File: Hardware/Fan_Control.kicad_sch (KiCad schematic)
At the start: 20 parts, among them Q1 PSMN8R5-40MSDX, Q3 PSMN8R5-40MSDX, U3 EMC2305-1-AP-TR

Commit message: BPS-Leader Schematic completed (mostly)
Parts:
- removed R14: 5k, symbol Device:R_US
- removed R15: 10k, symbol Device:R_US
- added R31, R35: 10k, Resistor_SMD:R_0603_1608Metric, symbol Device:R_US
- D4, D7: footprint UTSVT_Passive:MMDL101T1G -> UTSVT_Passives:MMDL101T1G
- R1, R13, R16, R17, R5: footprint (none) -> Resistor_SMD:R_0603_1608Metric
- R12: value 5k -> 10k; footprint (none) -> Resistor_SMD:R_0603_1608Metric
- R2: value 33k -> 10k; footprint (none) -> Resistor_SMD:R_0603_1608Metric
- R3, R4: value 10k -> 5k; footprint (none) -> Resistor_SMD:R_0603_1608Metric
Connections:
- net +3.3V: now also R1.2, R12.2, R31.1, R35.1; no longer R1.1, R12.1
- net CLK_PULLUP: now also R13.2; no longer R1.2
- net FAN_1_PWM: now also R12.1; no longer R5.2
- net FAN_1_TACH: now also R3.2; no longer R12.2, U3.6 (TACH1)
- net FAN_2_PWM: now also R1.1; no longer R13.2
- net FAN_2_TACH: now also R4.2; no longer U3.8 (TACH2)
- net FAN_ALERT: now also R5.2
- net FAN_SCL: now also R35.2; no longer R4.2
- net FAN_SDA: now also R31.2; no longer R3.2
- no-connect marks 6 -> 8
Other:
- note added: "Test to see if 100k pulldowns nessasaey"
- note removed: "Allows CLK pin to control fan default; See fig 1-2 for details"
- note removed: "Pull-Up Resistors"
- note removed: "Sets fan default to 50% see fig 1-1 for details"
- moved on the sheet: C1, C2, D4, D7, Fan1, Fan2, Q1, Q3, R16, R17, U3

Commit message: Small tweaks
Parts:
- R16, R17: now not fitted
- U3: footprint FanControl:QFN16_4x4MC_MCH -> (none)
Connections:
- net FAN_1_TACH: now also U3.6 (TACH1)
- net FAN_2_TACH: now also U3.8 (TACH2)
- no-connect marks 8 -> 6
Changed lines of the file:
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@@
 	)
 	(no_connect
-		(at 100.33 49.53)
-	)
-	(no_connect
 		(at 151.13 57.15)
 	)
@@
 		(at 151.13 44.45)
 	)
-	(no_connect
-		(at 100.33 54.61)
-	)
 	(wire
 		(pts
@@
 	(wire
 		(pts
+			(xy 87.63 49.53) (xy 100.33 49.53)
+		)
+		(stroke
+			(width 0)
+			(type default)
+		)
+	)
+	(wire
+		(pts
 			(xy 46.99 135.89) (xy 46.99 138.43)
 		)
@@
 	(wire
 		(pts
+			(xy 87.63 54.61) (xy 100.33 54.61)
+		)
+		(stroke
+			(width 0)
+			(type default)
+		)
+	)
+	(wire
+		(pts
 			(xy 151.13 49.53) (xy 154.94 49.53)
 		)
@@
 		)
 	)
+	(label "FAN_1_TACH"
+		(at 87.63 49.53 0)
+		(effects
+			(font
+				(size 1.27 1.27)
+			)
+			(justify left bottom)
+		)
+	)
 	(label "CLK_PULLUP"
 		(at 182.88 52.07 180)
@@
 		)
 	)
+	(label "FAN_2_TACH"
+		(at 87.63 54.61 0)
+		(effects
+			(font
+				(size 1.27 1.27)
+			)
+			(justify left bottom)
+		)
+	)
 	(label "FAN_1_FLYBACK"
 		(at 31.75 172.72 0)
@@
 			)
 		)
-		(property "Footprint" "FanControl:QFN16_4x4MC_MCH"
+		(property "Footprint" ""
 			(at 100.33 36.83 0)
 			(effects
@@
 		(in_bom yes)
 		(on_board yes)
-		(dnp no)
+		(dnp yes)
 		(fields_autoplaced yes)
 		(property "Reference" "R16"
@@
 		(in_bom yes)
 		(on_board yes)
-		(dnp no)
+		(dnp yes)
 		(fields_autoplaced yes)
 		(property "Reference" "R17"

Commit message: Very, very intial layout designed. Many issues. Too bad!
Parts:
- Fan1, Fan2: footprint (none) -> Connector_Molex:Molex_Nano-Fit_105309-xx03_1x03_P2.50mm_Vertical
- U3: footprint (none) -> SN74HC594DWG4:QFN16_4x4MC_MCH
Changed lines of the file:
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@@
 			)
 		)
-		(property "Footprint" ""
+		(property "Footprint" "Connector_Molex:Molex_Nano-Fit_105309-xx03_1x03_P2.50mm_Vertical"
 			(at 186.69 128.27 0)
 			(effects
@@
 			)
 		)
-		(property "Footprint" ""
+		(property "Footprint" "Connector_Molex:Molex_Nano-Fit_105309-xx03_1x03_P2.50mm_Vertical"
 			(at 250.19 128.27 0)
 			(effects
@@
 			)
 		)
-		(property "Footprint" ""
+		(property "Footprint" "SN74HC594DWG4:QFN16_4x4MC_MCH"
 			(at 100.33 36.83 0)
 			(effects

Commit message: Backup
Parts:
- U3: footprint SN74HC594DWG4:QFN16_4x4MC_MCH -> EMC2305-1-AP-TR:QFN65P400X400X90-17N-D
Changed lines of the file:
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@@
 			)
 		)
-		(property "Footprint" "SN74HC594DWG4:QFN16_4x4MC_MCH"
+		(property "Footprint" "EMC2305-1-AP-TR:QFN65P400X400X90-17N-D"
 			(at 100.33 36.83 0)
 			(effects

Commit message: small fixes
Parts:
- C1, C2: footprint Capacitor_SMD:C_0805_2012Metric -> Capacitor_SMD:C_0603_1608Metric; Manufactuerer (none) -> KEMET
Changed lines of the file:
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@@
 			)
 		)
-		(property "Footprint" "Capacitor_SMD:C_0805_2012Metric"
-			(at 44.45 45.72 0)
-			(effects
-				(font
-					(size 1.27 1.27)
-				)
-				(hide yes)
-			)
-		)
-		(property "Datasheet" "https://www.mouser.com/datasheet/2/447/KEM_C1006_X5R_SMD-3316465.pdf"
+		(property "Footprint" "Capacitor_SMD:C_0603_1608Metric"
+			(at 44.45 45.72 0)
+			(effects
+				(font
+					(size 1.27 1.27)
+				)
+				(hide yes)
+			)
+		)
+		(property "Datasheet" "https://www.mouser.com/datasheet/3/72/1/KEM_C1006_X5R_SMD.pdf"
 			(at 44.45 45.72 0)
 			(effects
@@
 			)
 		)
-		(property "Manufactuerer" ""
+		(property "Manufactuerer" "KEMET "
 			(at 44.45 45.72 0)
 			(effects
@@
 			)
 		)
-		(property "Footprint" "Capacitor_SMD:C_0805_2012Metric"
-			(at 49.53 45.72 0)
-			(effects
-				(font
-					(size 1.27 1.27)
-				)
-				(hide yes)
-			)
-		)
-		(property "Datasheet" "https://www.mouser.com/datasheet/2/447/KEM_C1006_X5R_SMD-3316465.pdf"
+		(property "Footprint" "Capacitor_SMD:C_0603_1608Metric"
+			(at 49.53 45.72 0)
+			(effects
+				(font
+					(size 1.27 1.27)
+				)
+				(hide yes)
+			)
+		)
+		(property "Datasheet" "https://www.mouser.com/datasheet/3/72/1/KEM_C1006_X5R_SMD.pdf"
 			(at 49.53 45.72 0)
 			(effects
@@
 			)
 		)
-		(property "Manufactuerer" ""
-			(at 49.53 45.72 0)
-			(effects
+		(property "Manufactuerer" "KEMET "
+			(at 49.53 45.72 0)
+			(effects

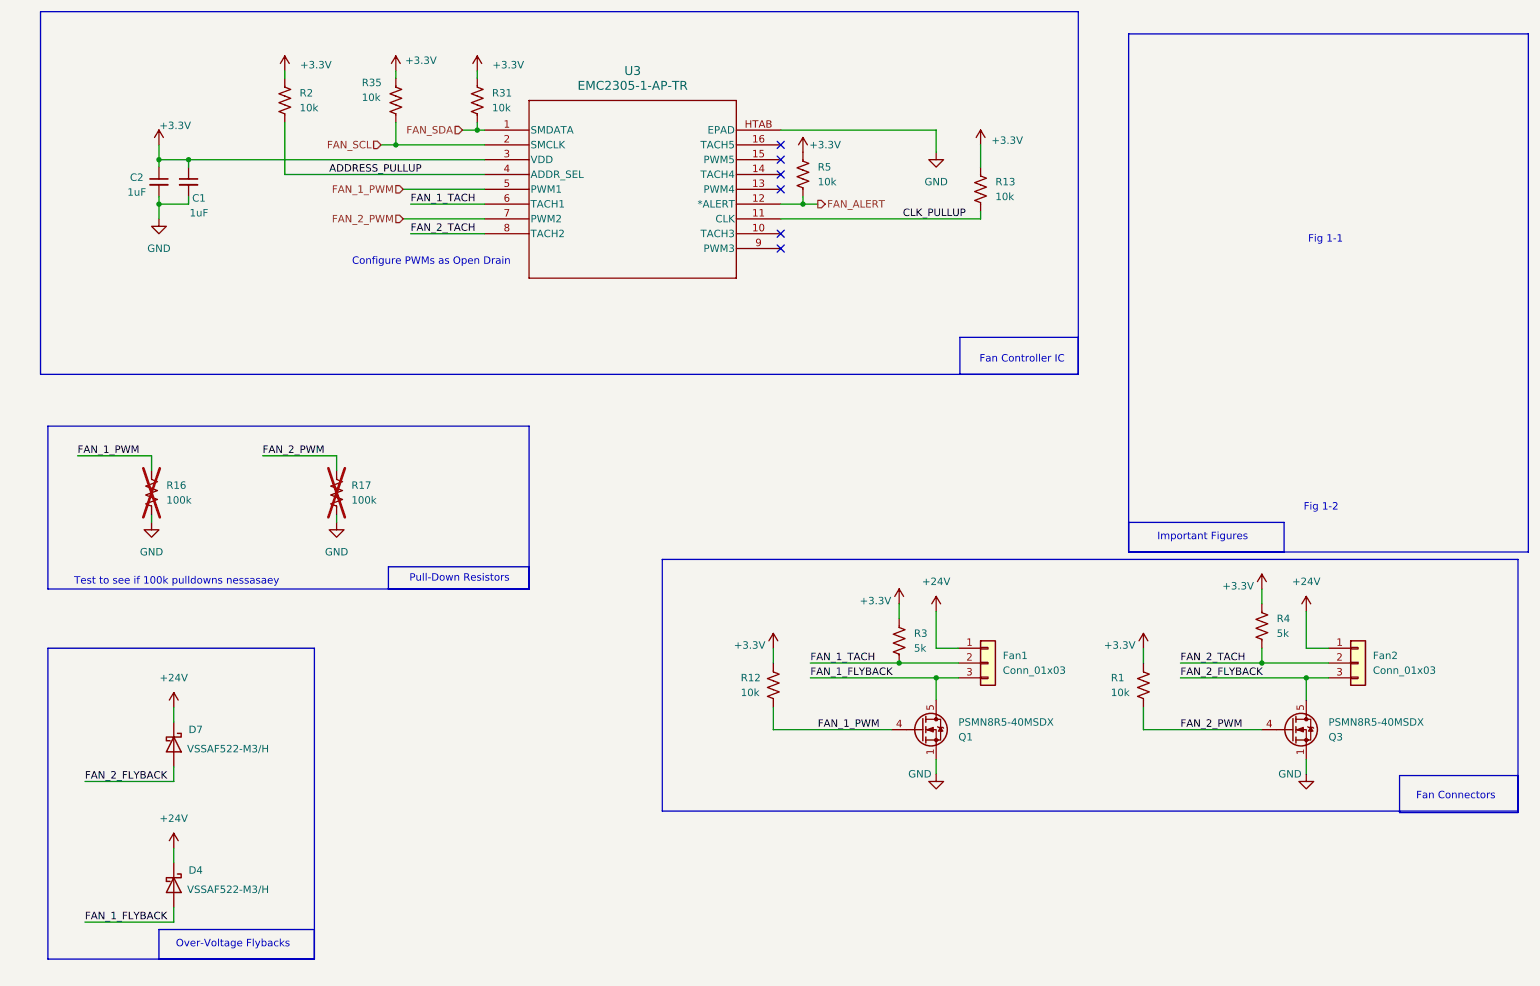
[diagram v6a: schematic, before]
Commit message: added BOM
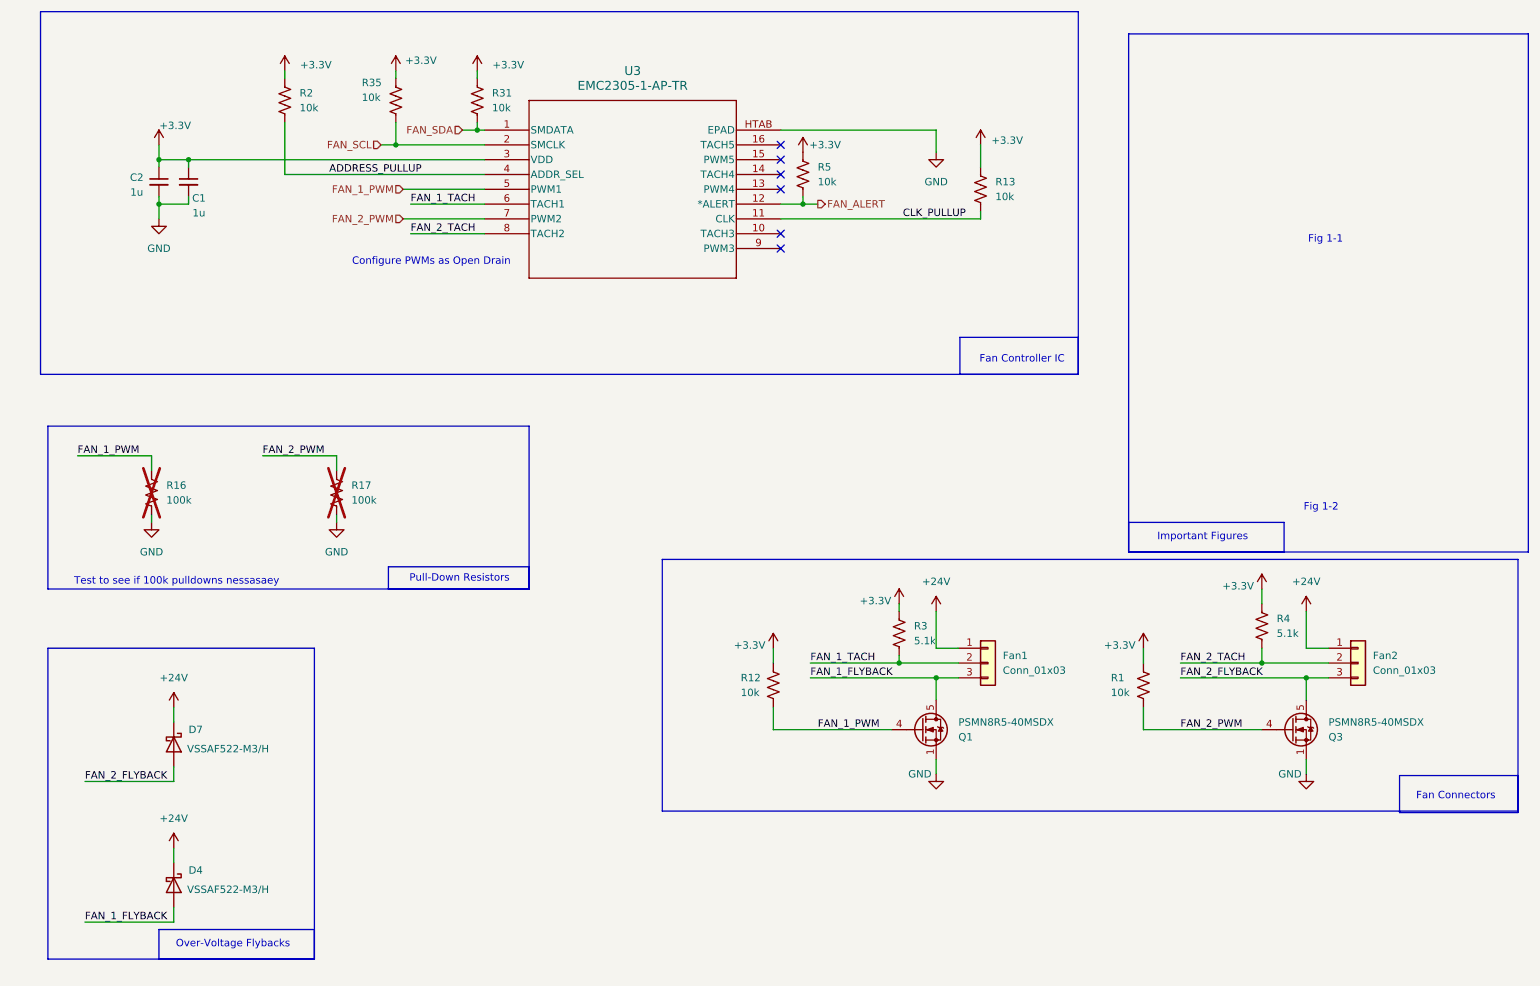
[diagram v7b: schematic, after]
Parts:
- C1, C2: value 1uF -> 1u; Manufactuerer KEMET -> TAIYO YUDEN; P/N C0805C105K5PACTU -> MLASU168SB5105KTNA01
- D4, D7: Manufactuerer (none) -> Vishay General Semiconductor; P/N (none) -> VSSAF522-M3/H
- Fan1, Fan2: Manufactuerer (none) -> Molex; P/N (none) -> 105309-1303
- Q1, Q3: Manufactuerer (none) -> Nexperia; P/N (none) -> PSMN8R5-40MSDX
- R1, R12, R13, R2, R31, R35, R5: Manufactuerer (none) -> Vishay; P/N (none) -> CRCW060310K0FKEI
- R16, R17: Manufactuerer (none) -> Vishay; P/N (none) -> CRCW0603100KFKEE
- R3, R4: value 5k -> 5.1k; Manufactuerer (none) -> Vishay; P/N (none) -> CRCW06035K10FKEC
- U3: Manufactuerer (none) -> Microchip Technology
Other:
- moved on the sheet: R3

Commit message: RevB PR (#14)
* RevB Schematic Update

* RevB Schematic revisions

* revB updates

* Schematic polishes, layout WIP

* circuit blocks designed, schematic updated

* unblocked SD card holder

* halfway laid-out

* unblocked SD card again

* small schematic changes

* intial layout design

* Updated LSOM footprint

* filled in copper holes. Name/REV/Date added

* RevB layout completed

* JLC Production Files

* added resistors

* replace silkscreen

* condensed custom lirbraries

* removed all unnessasary files and some nessasary ones
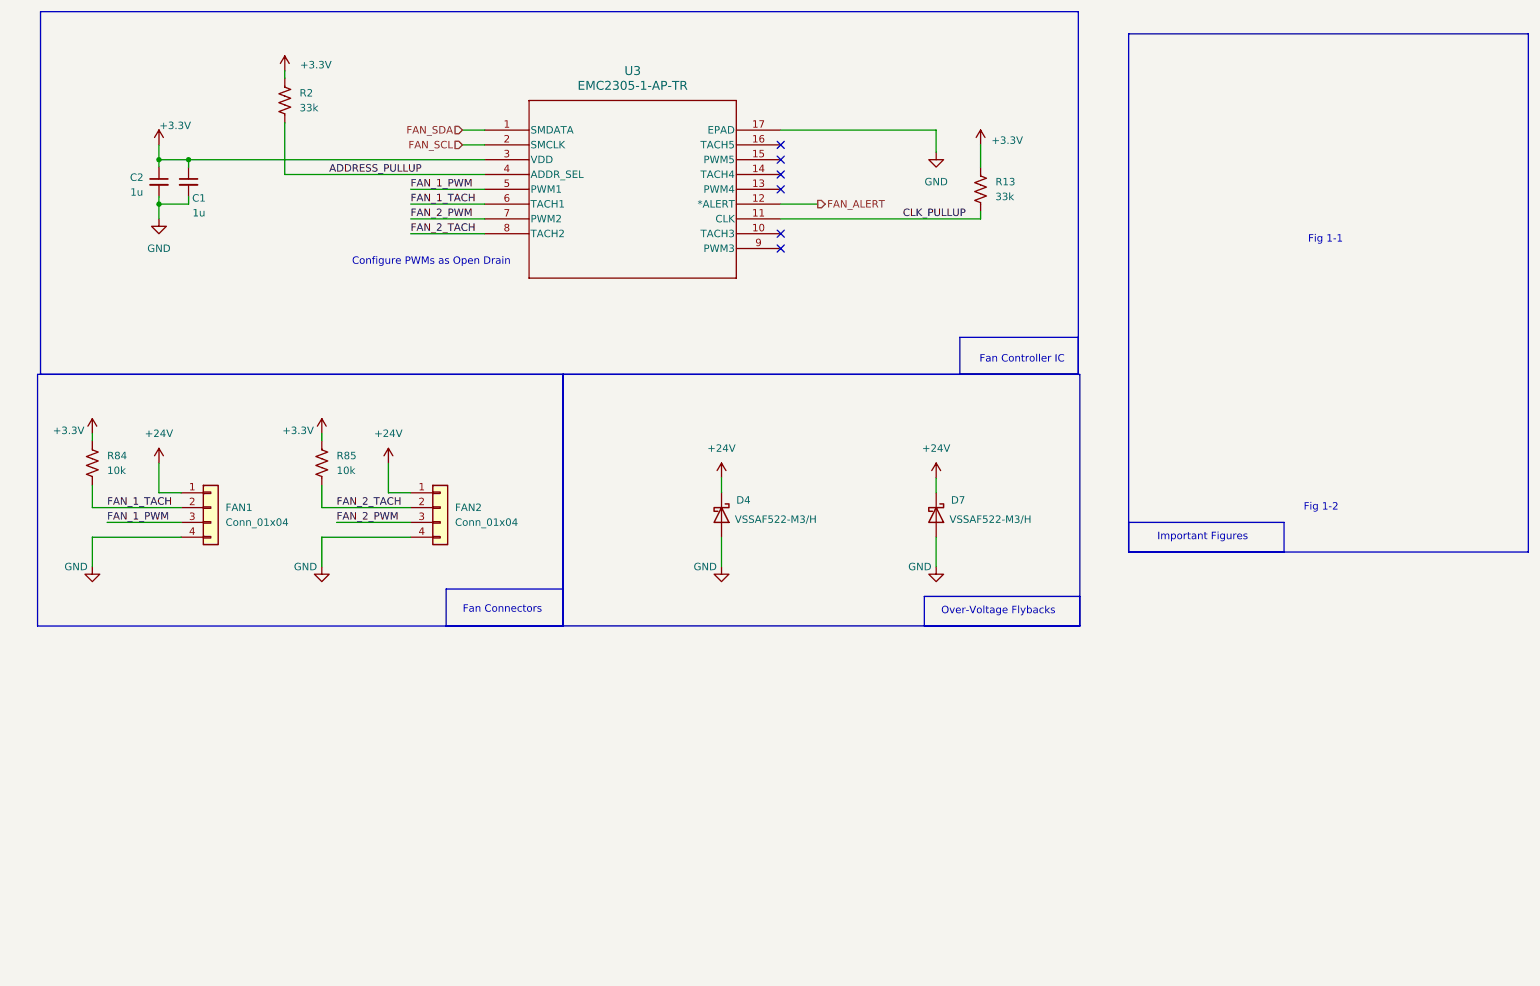
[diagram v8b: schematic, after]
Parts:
- removed Fan1, Fan2: Conn_01x03, Connector_Molex:Molex_Nano-Fit_105309-xx03_1x03_P2.50mm_Vertical, symbol Connector_Generic:Conn_01x03
- removed Q1, Q3: PSMN8R5-40MSDX, Package_TO_SOT_SMD:LFPAK33, symbol Transistor_FET:BUK7M27-80EX
- removed R1, R12, R31, R35, R5: 10k, Resistor_SMD:R_0603_1608Metric, symbol Device:R_US
- removed R16, R17: 100k, Resistor_SMD:R_0603_1608Metric, symbol Device:R_US
- removed R3, R4: 5.1k, Resistor_SMD:R_0603_1608Metric, symbol Device:R_US
- added FAN1, FAN2: Conn_01x04, Connector_Molex:Molex_Nano-Fit_105309-xx04_1x04_P2.50mm_Vertical, symbol Connector_Generic:Conn_01x04
- added R84, R85: 10k, Resistor_SMD:R_0603_1608Metric, symbol Device:R_US
- C1, C2: LCSC (none) -> C15849
- D4, D7: footprint UTSVT_Passives:MMDL101T1G -> CustomKiCad-Library:SODFL5226X100N; LCSC (none) -> C6326606
- R13, R2: value 10k -> 33k; LCSC (none) -> C844778
- U3: footprint EMC2305-1-AP-TR:QFN65P400X400X90-17N-D -> CustomKiCad-Library:QFN65P400X400X90-17N-D; LCSC (none) -> C621415
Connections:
- net FAN_1_FLYBACK is gone; now on net GND: D4.2 (A)
- net FAN_2_FLYBACK is gone; now on net GND: D7.2 (A)
- net +24V: now also FAN1.1 (Pin_1), FAN2.1 (Pin_1)
- net +3.3V: now also R84.1, R85.1
- net FAN_1_PWM: now also FAN1.3 (Pin_3)
- net FAN_1_TACH: now also FAN1.2 (Pin_2), R84.2
- net FAN_2_PWM: now also FAN2.3 (Pin_3)
- net FAN_2_TACH: now also FAN2.2 (Pin_2), R85.2
- net GND: now also U3.17 (EPAD), FAN1.4 (Pin_4), FAN2.4 (Pin_4); no longer U3.HTAB (EPAD)
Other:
- note removed: "Pull-Down Resistors"
- note removed: "Test to see if 100k pulldowns nessasaey"
- moved on the sheet: D4, D7
